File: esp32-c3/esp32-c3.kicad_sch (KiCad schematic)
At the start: 16 parts, among them J1 Conn_01x04_Socket, J4 Conn_01x02_Pin, J5 Conn_01x02_Pin, Q1 SS8050, Q2 SS8050, U1 ESP32-C3-MINI-1, U3 CPS125, U9 M24C02-RMN

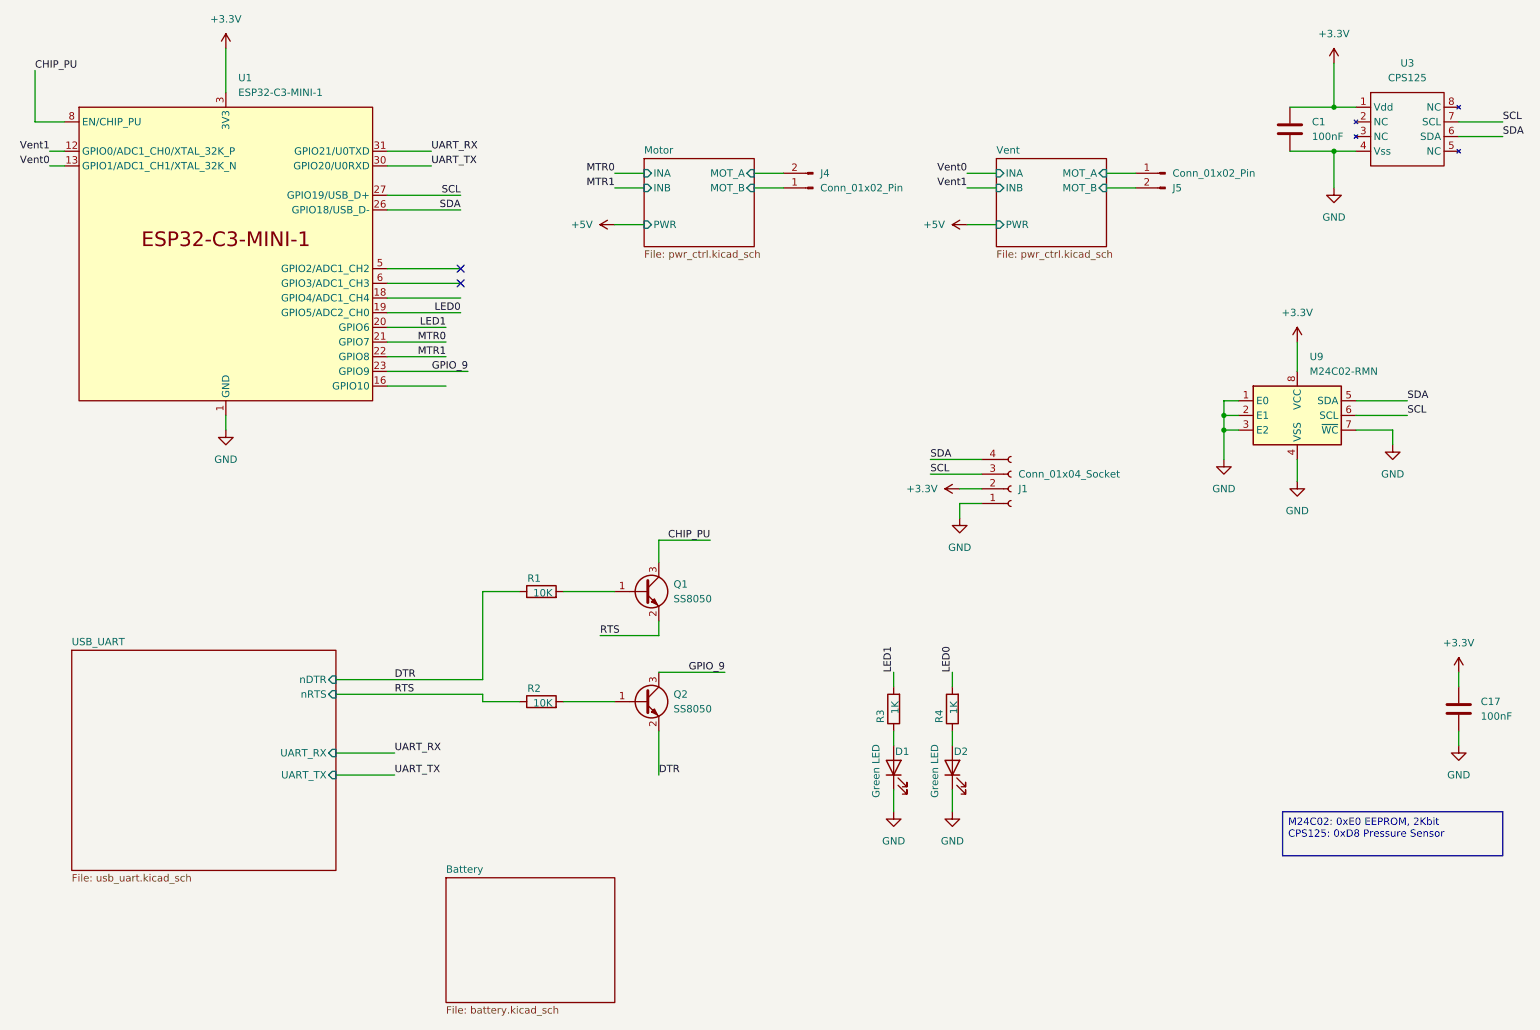
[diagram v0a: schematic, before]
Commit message: Fix Battery power and USB/UART connection, move vent around to accomodate enclosure
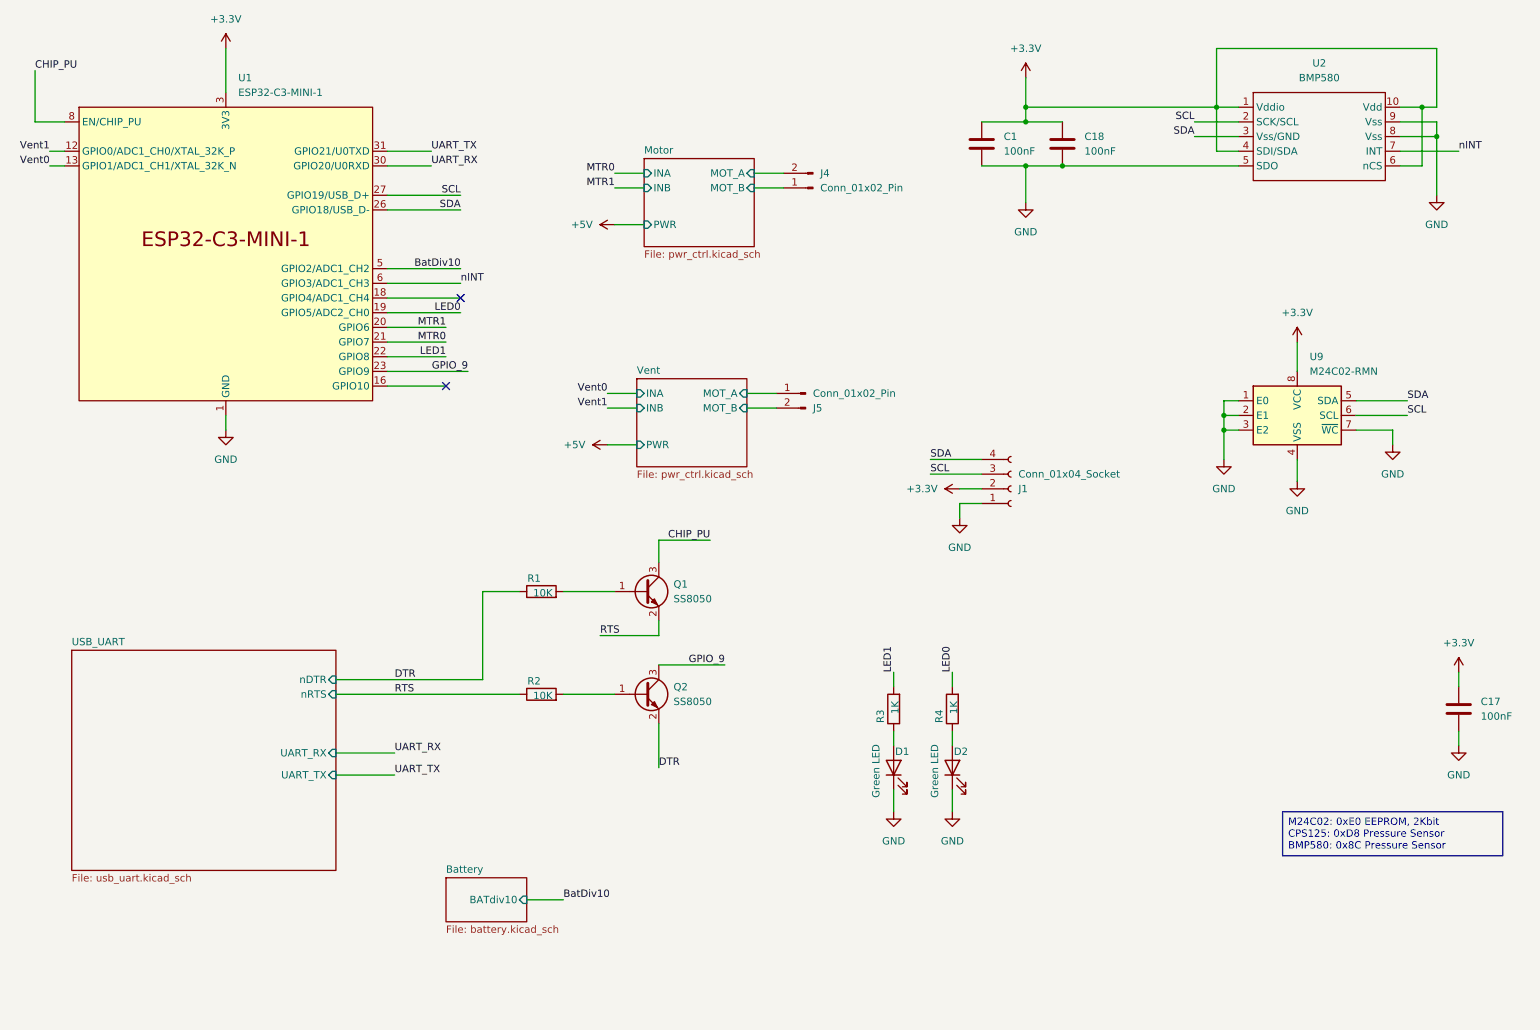
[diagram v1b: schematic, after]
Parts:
- removed U3: CPS125, local:CPS125, symbol local:CPS125
- added C18: 100nF, Capacitor_SMD:C_0402_1005Metric, symbol Device:C
- added U2: BMP580, local:BMP580_FP, symbol local:BMP580
- C1, C17: footprint Capacitor_SMD:C_0805_2012Metric -> Capacitor_SMD:C_0402_1005Metric
- U1: LCSC (none) -> C2934569
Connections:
- net +3.3V: now also C18.1, U2.1 (Vddio), U2.10 (Vdd), U2.4 (SDI/SDA), U2.6 (nCS)
- net GND: now also C18.2, U2.5 (SDO), U2.8 (Vss), U2.9 (Vss)
- net LED1: now also U1.22 (GPIO8); no longer U1.20 (GPIO6)
- net MTR1: now also U1.20 (GPIO6); no longer U1.22 (GPIO8)
- net SCL: now also U2.2 (SCK/SCL)
- net SDA: now also U2.3 (Vss/GND)
- net UART_RX: now also U1.30 (GPIO20/U0RXD); no longer U1.31 (GPIO21/U0TXD)
- net UART_TX: now also U1.31 (GPIO21/U0TXD); no longer U1.30 (GPIO20/U0RXD)
- net BatDiv10: now reaches U1.5 (GPIO2/ADC1_CH2)
- net nINT: now reaches U1.6 (GPIO3/ADC1_CH3)
- net nINT: now also U2.7 (INT)
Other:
- sheet Battery ports: added BATdiv10; removed none
- moved on the sheet: C1, J5, Q2, R2
